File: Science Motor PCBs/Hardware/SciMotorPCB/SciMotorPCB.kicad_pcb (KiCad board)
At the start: 2 copper layers, 34.3 x 40.6 mm, 3 parts, among them J1 Test_Point, J2 Test_Point

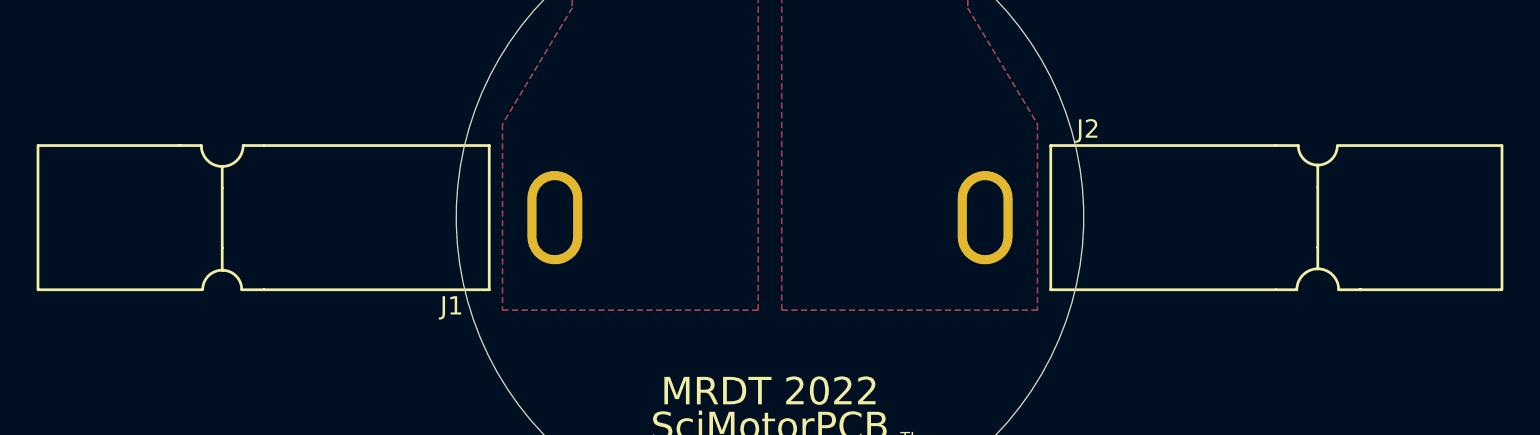
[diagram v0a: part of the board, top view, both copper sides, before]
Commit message: added pcb for J4, fixed the pitches
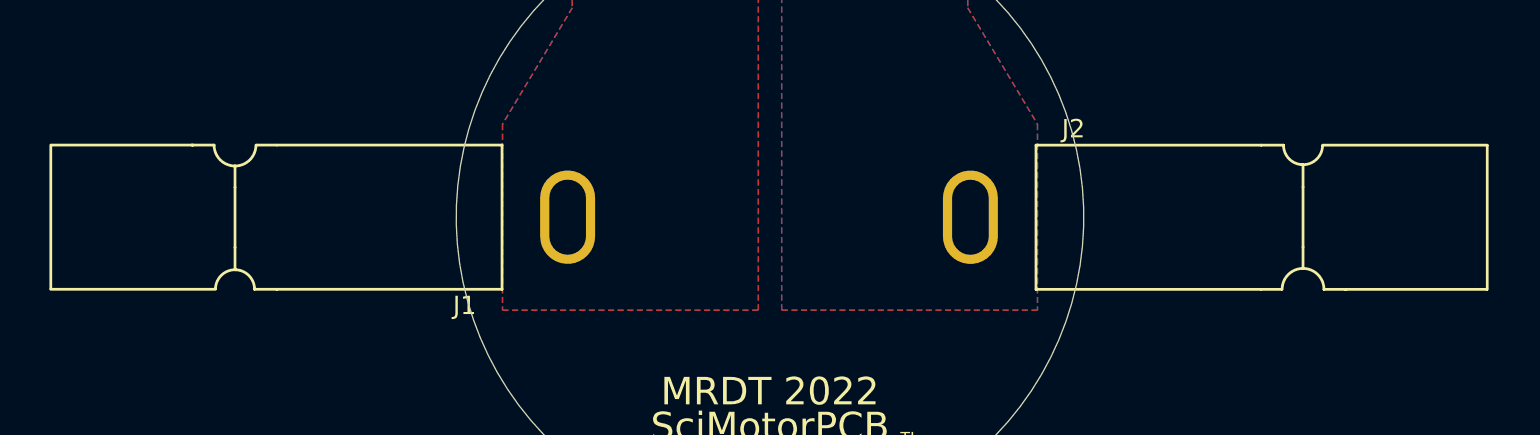
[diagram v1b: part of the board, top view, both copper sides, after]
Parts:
- moved J2 0.81 mm to (167.5, 96.0)
- moved J1 0.70 mm to (146.1, 95.8)

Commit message: gerbs added and zipped
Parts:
- added J1: Test_Point, MRDT_Connectors:Square_Anderson_1_H, F.Cu at (164.3, 103.7)
- added J2: Test_Point, MRDT_Connectors:Square_Anderson_1_H, F.Cu at (149.3, 88.4)
- moved Conn1 0.38 mm to (156.8, 75.2)
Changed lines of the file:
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@@
   (general
     (thickness 1.6)
-    (drawings 32)
+    (drawings 33)
     (tracks 0)
     (zones 0)
-    (modules 3)
+    (modules 5)
     (nets 3)
   )
@@
     (mod_text_size 1 1)
     (mod_text_width 0.15)
-    (pad_size 1.524 1.524)
-    (pad_drill 0.762)
+    (pad_size 2.999999 5.1)
+    (pad_drill 2)
     (pad_to_mask_clearance 0)
     (aux_axis_origin 0 0)
@@
       (outputformat 1)
       (mirror false)
-      (drillshape 1)
+      (drillshape 0)
       (scaleselection 1)
-      (outputdirectory ""))
+      (outputdirectory "../../Manufacturing/Gerbs/"))
   )
   (net 0 "")
@@
     (add_net "Net-(Conn1-Pad2)")
   )
+  (module MRDT_Connectors:Square_Anderson_1_H (layer F.Cu)
+    (at 149.310625 88.380008 315)
+    (fp_text reference J2 (at -5.9 4.95 135) (layer F.SilkS)
+      (effects (font (size 1 1) (thickness 0.15)))
+    )
+    (fp_text value Test_Point (at -17.2 -4.65 135) (layer F.Fab)
+      (effects (font (size 1 1) (thickness 0.15)))
+    )
+    (fp_line (start -16.1496 -3.814) (end -3.856 -3.814) (layer F.SilkS) (width 0.15))
+    (fp_line (start -18.4356 1.774) (end -18.4356 2.917) (layer F.SilkS) (width 0.15))
+    (fp_line (start -18.4356 -2.671) (end -18.4356 -1.5026) (layer F.SilkS) (width 0.15))
+    (fp_line (start -16.175 -3.814) (end -17.2672 -3.814) (layer F.SilkS) (width 0.15))
+    (fp_line (start -28.4686 -3.814) (end -20.7216 -3.814) (layer F.SilkS) (width 0.15))
+    (fp_line (start -3.856 4.06) (end -3.856 -3.814) (layer F.SilkS) (width 0.15))
+    (fp_line (start -28.494 -3.814) (end -28.494 4.0346) (layer F.SilkS) (width 0.15))
+    (fp_line (start -19.5786 -3.814) (end -20.7978 -3.814) (layer F.SilkS) (width 0.15))
+    (fp_line (start -16.1496 4.06) (end -3.856 4.06) (layer F.SilkS) (width 0.15))
+    (fp_line (start -18.4356 1.774) (end -18.4356 -1.5026) (layer F.SilkS) (width 0.15))
+    (fp_line (start -28.494 4.06) (end -19.5024 4.06) (layer F.SilkS) (width 0.15))
+    (fp_line (start -17.3688 4.06) (end -16.1496 4.06) (layer F.SilkS) (width 0.15))
+    (fp_arc (start -18.4356 -3.814) (end -18.4356 -2.671) (angle 90) (layer F.SilkS) (width 0.15))
+    (fp_arc (start -18.4356 4.06) (end -18.4356 2.9932) (angle 90) (layer F.SilkS) (width 0.15))
+    (fp_arc (start -18.4356 -3.814) (end -17.2926 -3.814) (angle 90) (layer F.SilkS) (width 0.15))
+    (fp_arc (start -18.4356 4.06) (end -19.5024 4.0092) (angle 90) (layer F.SilkS) (width 0.15))
+    (pad 1 thru_hole oval (at -0.2746 0.123001 315) (size 2.999999 5.1) (drill oval 2 4.099999) (layers *.Cu *.Mask F.Paste)
+      (net 1 "Net-(Conn1-Pad1)"))
+  )
+  (module MRDT_Connectors:Square_Anderson_1_H (layer F.Cu)
+    (at 164.295915 103.718851 135)
+    (fp_text reference J1 (at -5.9 4.95 135) (layer F.SilkS)
+      (effects (font (size 1 1) (thickness 0.15)))
+    )
+    (fp_text value Test_Point (at -17.2 -4.65 135) (layer F.Fab)
+      (effects (font (size 1 1) (thickness 0.15)))
+    )
+    (fp_line (start -16.1496 -3.814) (end -3.856 -3.814) (layer F.SilkS) (width 0.15))
+    (fp_line (start -18.4356 1.774) (end -18.4356 2.917) (layer F.SilkS) (width 0.15))
+    (fp_line (start -18.4356 -2.671) (end -18.4356 -1.5026) (layer F.SilkS) (width 0.15))
+    (fp_line (start -16.175 -3.814) (end -17.2672 -3.814) (layer F.SilkS) (width 0.15))
+    (fp_line (start -28.4686 -3.814) (end -20.7216 -3.814) (layer F.SilkS) (width 0.15))
+    (fp_line (start -3.856 4.06) (end -3.856 -3.814) (layer F.SilkS) (width 0.15))
+    (fp_line (start -28.494 -3.814) (end -28.494 4.0346) (layer F.SilkS) (width 0.15))
+    (fp_line (start -19.5786 -3.814) (end -20.7978 -3.814) (layer F.SilkS) (width 0.15))
+    (fp_line (start -16.1496 4.06) (end -3.856 4.06) (layer F.SilkS) (width 0.15))
+    (fp_line (start -18.4356 1.774) (end -18.4356 -1.5026) (layer F.SilkS) (width 0.15))
+    (fp_line (start -28.494 4.06) (end -19.5024 4.06) (layer F.SilkS) (width 0.15))
+    (fp_line (start -17.3688 4.06) (end -16.1496 4.06) (layer F.SilkS) (width 0.15))
+    (fp_arc (start -18.4356 -3.814) (end -18.4356 -2.671) (angle 90) (layer F.SilkS) (width 0.15))
+    (fp_arc (start -18.4356 4.06) (end -18.4356 2.9932) (angle 90) (layer F.SilkS) (width 0.15))
+    (fp_arc (start -18.4356 -3.814) (end -17.2926 -3.814) (angle 90) (layer F.SilkS) (width 0.15))
+    (fp_arc (start -18.4356 4.06) (end -19.5024 4.0092) (angle 90) (layer F.SilkS) (width 0.15))
+    (pad 1 thru_hole oval (at -0.2746 0.123001 135) (size 2.999999 5.1) (drill oval 2 4.099999) (layers *.Cu *.Mask F.Paste)
+      (net 2 "Net-(Conn1-Pad2)"))
+  )
   (module MRDT_Connectors:Square_Anderson_2_V_Side_By_Side (layer B.Cu)
-    (at 156.845 75.565)
+    (at 156.845 75.184)
     (fp_text reference Conn1 (at 6.2 -6.3 180) (layer B.SilkS)
       (effects (font (size 1 1) (thickness 0.15)) (justify mirror))
@@
       (net 2 "Net-(Conn1-Pad2)"))
   )
+  (gr_text "MRDT 2022" (at 156.845 95.25) (layer B.SilkS)
+    (effects (font (size 1.5 1.5) (thickness 0.3)) (justify mirror))
+  )
+  (gr_text TL (at 149.225 97.79) (layer B.SilkS)
+    (effects (font (size 0.635 0.635) (thickness 0.0762)) (justify mirror))
+  )
+  (gr_text SciMotorPCB (at 156.845 97.155) (layer B.SilkS)
+    (effects (font (size 1.5 1.5) (thickness 0.3)) (justify mirror))
+  )
+  (gr_circle (center 156.845 95.885) (end 168.021 95.8215) (layer Dwgs.User) (width 0.15))
   (dimension 10.668 (width 0.15) (layer Dwgs.User)
     (gr_text "0.4200 in" (at 151.511 103.535) (layer Dwgs.User)
@@
   )
   (gr_arc (start 156.845 95.885) (end 145.415001 83.121501) (angle -275.939028) (layer Edge.Cuts) (width 0.05))
-  (gr_text TL (at 149.225 107.95) (layer B.SilkS)
-    (effects (font (size 0.635 0.635) (thickness 0.0762)) (justify mirror))
-  )
-  (gr_text TL (at 164.465 107.95) (layer F.SilkS)
+  (gr_text TL (at 164.465 97.79) (layer F.SilkS)
     (effects (font (size 0.635 0.635) (thickness 0.0762)))
   )
-  (gr_text "MRDT 2022" (at 156.845 105.41) (layer B.SilkS)
-    (effects (font (size 1.5 1.5) (thickness 0.3)) (justify mirror))
-  )
-  (gr_text SciMotorPCB (at 156.845 107.315) (layer B.SilkS)
-    (effects (font (size 1.5 1.5) (thickness 0.3)) (justify mirror))
-  )
-  (gr_text SciMotorPCB (at 156.845 107.315) (layer F.SilkS)
+  (gr_text SciMotorPCB (at 156.845 97.155) (layer F.SilkS)
     (effects (font (size 1.5 1.5) (thickness 0.3)))
   )
-  (gr_text "MRDT 2022" (at 156.845 105.41) (layer F.SilkS)
+  (gr_text "MRDT 2022" (at 156.845 95.25) (layer F.SilkS)
     (effects (font (size 1.5 1.5) (thickness 0.3)))
   )
@@
     (polygon
       (pts
-        (xy 167.64 84.455) (xy 171.45 90.805) (xy 171.45 100.965) (xy 157.48 100.965) (xy 157.48 73.025)
-        (xy 167.64 73.025)
+        (xy 175.26 81.915) (xy 178.435 92.3925) (xy 178.435 115.8875) (xy 157.48 114.3) (xy 157.48 71.12)
+        (xy 167.64 71.12)
       )
     )
@@
     (polygon
       (pts
-        (xy 167.64 84.455) (xy 171.45 90.805) (xy 171.45 100.965) (xy 157.48 100.965) (xy 157.48 73.025)
-        (xy 167.64 73.025)
+        (xy 174.625 82.55) (xy 180.0225 89.535) (xy 177.165 114.935) (xy 157.48 114.3) (xy 157.48 70.485)
+        (xy 167.64 70.485)
       )
     )
@@
     (polygon
       (pts
-        (xy 146.05 84.455) (xy 142.24 90.805) (xy 142.24 100.965) (xy 156.21 100.965) (xy 156.21 73.025)
-        (xy 146.05 73.025)
+        (xy 140.97 83.82) (xy 137.795 90.805) (xy 137.795 114.935) (xy 156.21 114.935) (xy 156.21 70.485)
+        (xy 146.05 70.485)
       )
     )
@@
     (polygon
       (pts
-        (xy 146.05 84.455) (xy 142.24 90.805) (xy 142.24 100.965) (xy 156.21 100.965) (xy 156.21 73.025)
-        (xy 146.05 73.025)
+        (xy 140.335 84.1375) (xy 137.795 91.7575) (xy 140.335 116.5225) (xy 156.21 114.935) (xy 156.21 70.96125)
+        (xy 142.5575 71.27875)
       )
     )
